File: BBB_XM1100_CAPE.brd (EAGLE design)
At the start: 54.6 x 71.8 mm, 24 parts, among them U2 MIC5225-3.3

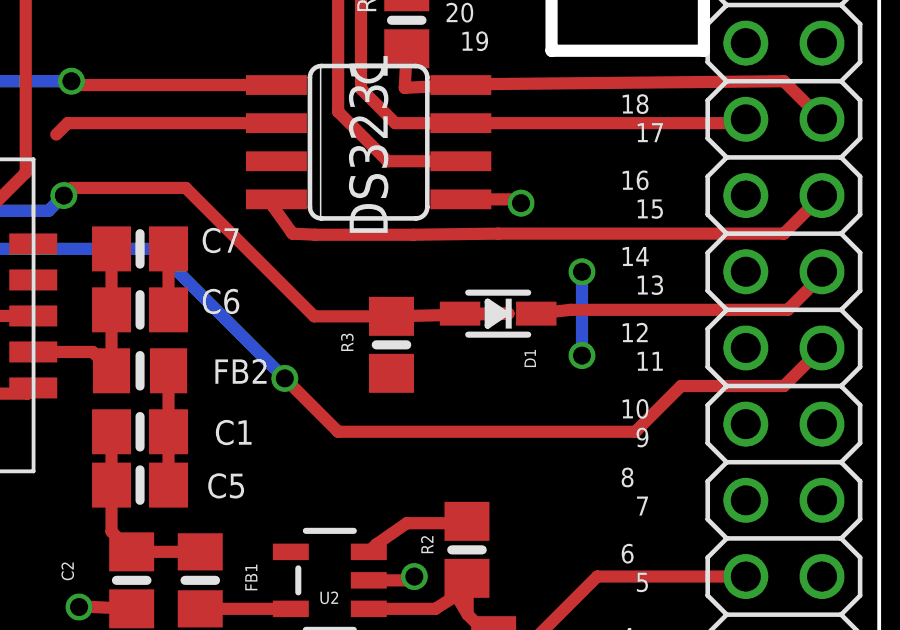
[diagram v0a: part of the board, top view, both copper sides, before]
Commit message: moved errant wire on XM1100 layout
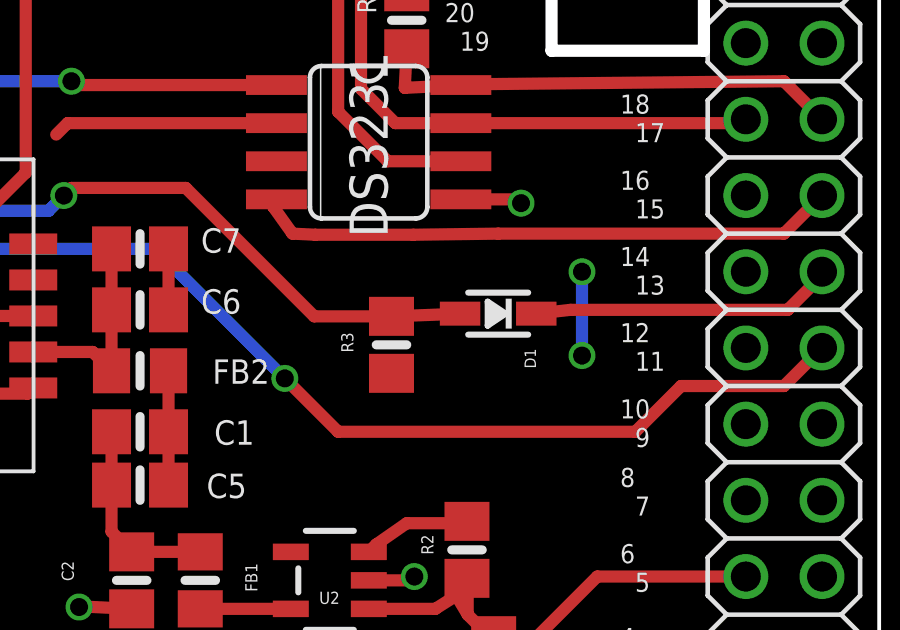
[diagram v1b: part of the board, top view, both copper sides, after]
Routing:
- net RX_3V: track 29.6 -> 26.6 mm
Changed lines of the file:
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@@
 <contactref element="D1" pad="A"/>
 <contactref element="U$3" pad="P$17"/>
-<wire x1="43.434" y1="18.415" x2="45.048" y2="18.415" width="0.4064" layer="1"/>
-<wire x1="45.048" y1="18.415" x2="41.148" y2="18.325" width="0.4064" layer="1"/>
+<wire x1="43.434" y1="18.415" x2="43.524" y2="18.415" width="0.4064" layer="1"/>
+<wire x1="43.524" y1="18.415" x2="41.148" y2="18.325" width="0.4064" layer="1"/>
 <wire x1="41.148" y1="18.325" x2="38.571" y2="18.325" width="0.4064" layer="1"/>
 <wire x1="38.571" y1="18.325" x2="34.29" y2="22.606" width="0.4064" layer="1"/>
